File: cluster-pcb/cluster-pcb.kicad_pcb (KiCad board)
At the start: 4 copper layers, 60 x 160 mm, 77 parts, among them J1001 FFC_P1mm_BOT_RA_SMD, J1101 FFC_P1mm_BOT_RA_SMD, J501 FFC_P1mm_BOT_RA_SMD, J601 FFC_P1mm_BOT_RA_SMD, J701 FFC_P1mm_BOT_RA_SMD, J801 FFC_P1mm_BOT_RA_SMD, J901 FFC_P1mm_BOT_RA_SMD, Q301 MOSFET-N-CH-EN_100V_260mA, Q302 MOSFET-P-CH-EN_60V_50A, T301 TERM_BLK_HDR_2POS_90DEG_0.2IN, U1001 MAX13431E, U1101 MAX13431E, U301 TPSM365R6V5RDNR, U501 MAX13431E, U601 MAX13431E, U701 MAX13431E, U801 MAX13431E, U901 MAX13431E

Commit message: First steps towards v1.1
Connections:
- C303 pad 1: /VCC -> /power/VDD
- U301 pad 11: /VCC -> /power/VDD
- U301 pad 8: /VCC -> /power/VDD
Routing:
- net /VCC: track 160.5 -> 120.2 mm
- net /power/VDD: track 0.00 -> 12.8 mm
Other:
- board text added: "cluster-pcb v1.1 2024/08"
- board text removed: "cluster-pcb v1.0 2024/07"
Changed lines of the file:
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@@
   (title_block
     (title "cluster-pcb")
-    (date "2024-07-26")
-    (rev "1.0")
+    (date "2024-08-19")
+    (rev "1.1")
     (company "Howard Hughes Medical Institute")
   )
@@
   (net 77 "unconnected-(U301-BOOT-Pad7)")
   (net 78 "Net-(Q301-D)")
+  (net 79 "/power/VDD")
   (footprint "Janelia:FIDUCIAL_0.5mm_Mask1mm" (layer "F.Cu")
     (at 77.4 31.6)
@@
       (stroke (width 0.1) (type solid)) (layer "F.Fab"))
     (pad "1" smd roundrect (at -0.48 0 270) (size 0.56 0.62) (layers "F.Cu" "F.Paste" "F.Mask") (roundrect_rratio 0.25)
-      (net 43 "/VCC") (pintype "passive"))
+      (net 79 "/power/VDD") (pintype "passive"))
     (pad "2" smd roundrect (at 0.48 0 270) (size 0.56 0.62) (layers "F.Cu" "F.Paste" "F.Mask") (roundrect_rratio 0.25)
       (net 1 "/GND") (pintype "passive"))
@@
       (net 77 "unconnected-(U301-BOOT-Pad7)") (pinfunction "BOOT") (pintype "unspecified+no_connect"))
     (pad "8" smd rect (at 1.4 -1.962 270) (size 1.2 0.475) (layers "F.Cu")
-      (net 43 "/VCC") (pinfunction "VCC") (pintype "unspecified"))
+      (net 79 "/power/VDD") (pinfunction "VCC") (pintype "unspecified"))
     (pad "9" smd rect (at 0.499999 -2.049998 270) (size 0.349999 0.900001) (layers "F.Cu")
       (net 34 "/+5V") (pinfunction "BIAS") (pintype "unspecified"))
@@
       (net 1 "/GND") (pinfunction "GND") (pintype "power_in"))
     (pad "11" smd rect (at -0.499999 -2.049998 270) (size 0.349999 0.900001) (layers "F.Cu")
-      (net 43 "/VCC") (pinfunction "MODE_SYNC") (pintype "unspecified"))
+      (net 79 "/power/VDD") (pinfunction "MODE_SYNC") (pintype "unspecified"))
     (model "${KICAD_JANELIA_LIBRARY}/3dmodels/Janelia.3dshapes/TPSM365R6V5RDNR.step"
       (offset (xyz 0 0 0))
@@
     (effects (font (size 3 3) (thickness 0.75) bold))
   )
-  (gr_text "cluster-pcb\nv1.0 2024/07" (at 92.4 161.6) (layer "F.SilkS")
+  (gr_text "cluster-pcb\nv1.1 2024/08" (at 92.4 161.6) (layer "F.SilkS")
     (effects (font (size 2 2) (thickness 0.5) bold))
   )
@@
   (segment (start 107.12 36.56) (end 104.1925 33.6325) (width 0.6) (layer "F.Cu") (net 42))
   (segment (start 76.92 39.6) (end 76.92 40.12) (width 0.6) (layer "F.Cu") (net 42))
-  (segment (start 79.419999 43.100001) (end 80.4 42.12) (width 0.3) (layer "F.Cu") (net 43))
   (segment (start 110.4375 82.6) (end 110.4375 102.6) (width 2) (layer "F.Cu") (net 43))
   (segment (start 110.4375 102.6) (end 110.4375 122.6) (width 2) (layer "F.Cu") (net 43))
-  (segment (start 82.4 44.1) (end 82.4 43.1) (width 0.3) (layer "F.Cu") (net 43))
-  (segment (start 81.42 42.12) (end 80.4 42.12) (width 0.3) (layer "F.Cu") (net 43))
-  (segment (start 80.75 46.75) (end 82.4 45.1) (width 0.3) (layer "F.Cu") (net 43))
-  (segment (start 83.64 42.86) (end 109.4 42.86) (width 0.3) (layer "F.Cu") (net 43))
-  (segment (start 78.362 45) (end 78.362 45.981239) (width 0.3) (layer "F.Cu") (net 43))
   (segment (start 110.4375 48.6) (end 110.4375 62.6) (width 2) (layer "F.Cu") (net 43))
-  (segment (start 82.4 45.1) (end 82.4 44.1) (width 0.3) (layer "F.Cu") (net 43))
-  (segment (start 82.4 44.1) (end 83.64 42.86) (width 0.3) (layer "F.Cu") (net 43))
-  (segment (start 82.4 43.1) (end 81.42 42.12) (width 0.3) (layer "F.Cu") (net 43))
-  (segment (start 79.130761 46.75) (end 80.75 46.75) (width 0.3) (layer "F.Cu") (net 43))
   (segment (start 110.4375 48.6) (end 110.4375 43.8975) (width 2) (layer "F.Cu") (net 43))
   (segment (start 110.4375 43.8975) (end 109.4 42.86) (width 2) (layer "F.Cu") (net 43))
-  (segment (start 78.362 45.981239) (end 79.130761 46.75) (width 0.3) (layer "F.Cu") (net 43))
   (segment (start 110.4375 122.6) (end 110.4375 142.6) (width 2) (layer "F.Cu") (net 43))
   (segment (start 110.4375 142.6) (end 110.4375 162.6) (width 2) (layer "F.Cu") (net 43))
   (segment (start 110.4375 62.6) (end 110.4375 82.6) (width 2) (layer "F.Cu") (net 43))
-  (segment (start 78.449998 43.100001) (end 79.419999 43.100001) (width 0.3) (layer "F.Cu") (net 43))
   (segment (start 122.320001 30.5337) (end 120.479999 30.5337) (width 2) (layer "F.Cu") (net 44))
   (segment (start 120.479999 30.5337) (end 114.7188 30.5337) (width 2) (layer "F.Cu") (net 44))
@@
   (segment (start 78.4625 65.0475) (end 79.4 64.11) (width 0.3) (layer "F.Cu") (net 78))
   (segment (start 78.4625 66.6) (end 78.4625 65.0475) (width 0.3) (layer "F.Cu") (net 78))
+  (segment (start 79.419999 43.100001) (end 80.4 42.12) (width 0.3) (layer "F.Cu") (net 79))
+  (segment (start 82.4 44.1) (end 82.4 43.1) (width 0.3) (layer "F.Cu") (net 79))
+  (segment (start 81.42 42.12) (end 80.4 42.12) (width 0.3) (layer "F.Cu") (net 79))
+  (segment (start 80.75 46.75) (end 82.4 45.1) (width 0.3) (layer "F.Cu") (net 79))
+  (segment (start 78.362 45) (end 78.362 45.981239) (width 0.3) (layer "F.Cu") (net 79))
+  (segment (start 82.4 45.1) (end 82.4 44.1) (width 0.3) (layer "F.Cu") (net 79))
+  (segment (start 82.4 43.1) (end 81.42 42.12) (width 0.3) (layer "F.Cu") (net 79))
+  (segment (start 79.130761 46.75) (end 80.75 46.75) (width 0.3) (layer "F.Cu") (net 79))
+  (segment (start 78.362 45.981239) (end 79.130761 46.75) (width 0.3) (layer "F.Cu") (net 79))
+  (segment (start 78.449998 43.100001) (end 79.419999 43.100001) (width 0.3) (layer "F.Cu") (net 79))
   (zone (net 43) (net_name "/VCC") (layer "F.Cu") (hatch edge 0.5)
     (priority 2)

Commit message: Update to version 1.1
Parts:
- removed D1001, D1101, D501, D601, D701, D801, D901: D_Zener_47V_1W, Janelia:D_SMA
- removed D1002, D1102, D502, D602, D702, D802, D902: D, Janelia:D_SMB
- removed R1001, R1101, R501, R601, R701, R801, R901: 0.24, Janelia:R_2512_6332Metric
- added C305: 47uF_10V, Janelia:C_0805_2012Metric, F.Cu at (76.4, 49.1)
- added D302: LED_RED, Janelia:LED_0402-1005_KNB, F.Cu at (123.9, 23.4)
- added R303: 2.32k, Janelia:R_0805_2012Metric, F.Cu at (121.2, 23.4)
- Q301: value MOSFET-N-CH-EN_100V_260mA -> Transistor_BJT_NPN
- R301: value 1k -> 10.0k
- R302: value 3.6k -> 2.7k
- moved C304 4.72 mm to (76.4, 47.1), turned to 0 degrees
- moved C301 3.91 mm to (80.4, 39.1), turned to -90 degrees
- moved C303 3.04 mm to (79.9, 45.6), turned to 90 degrees
- moved Q301 2.00 mm to (79.4, 68.6), turned to -90 degrees
- moved R302 1.50 mm to (79.4, 65.1), turned to 0 degrees
- moved C1001 1.00 mm to (121.4, 114.6)
- moved C1002 1.00 mm to (123.4, 114.6)
- moved C1101 1.00 mm to (121.4, 154.6)
- moved C1102 1.00 mm to (123.4, 154.6)
- moved C501 1.00 mm to (121.4, 34.6)
- moved C502 1.00 mm to (123.4, 34.6)
- moved C601 1.00 mm to (121.4, 54.6)
- moved C602 1.00 mm to (123.4, 54.6)
- moved C701 1.00 mm to (121.4, 74.6)
- moved C702 1.00 mm to (123.4, 74.6)
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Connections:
- J1001 pad 1: /prism-4/VCC -> /VCC
- J1001 pad 2: /prism-4/VCC -> /VCC
- J1001 pad 3: /prism-4/VCC -> /VCC
- J1001 pad 4: /prism-4/VCC -> /VCC
- J1101 pad 1: /prism-6/VCC -> /VCC
- J1101 pad 2: /prism-6/VCC -> /VCC
- J1101 pad 3: /prism-6/VCC -> /VCC
- J1101 pad 4: /prism-6/VCC -> /VCC
- J501 pad 1: /prism-0/VCC -> /VCC
- J501 pad 2: /prism-0/VCC -> /VCC
- J501 pad 3: /prism-0/VCC -> /VCC
- J501 pad 4: /prism-0/VCC -> /VCC
- J601 pad 1: /prism-1/VCC -> /VCC
- J601 pad 2: /prism-1/VCC -> /VCC
- J601 pad 3: /prism-1/VCC -> /VCC
- J601 pad 4: /prism-1/VCC -> /VCC
- J701 pad 1: /prism-2/VCC -> /VCC
- J701 pad 2: /prism-2/VCC -> /VCC
- J701 pad 3: /prism-2/VCC -> /VCC
- J701 pad 4: /prism-2/VCC -> /VCC
- J801 pad 1: /prism-3/VCC -> /VCC
- J801 pad 2: /prism-3/VCC -> /VCC
- J801 pad 3: /prism-3/VCC -> /VCC
- J801 pad 4: /prism-3/VCC -> /VCC
- J901 pad 1: /prism-5/VCC -> /VCC
- J901 pad 2: /prism-5/VCC -> /VCC
- J901 pad 3: /prism-5/VCC -> /VCC
- J901 pad 4: /prism-5/VCC -> /VCC
- Q301 pad 2: /GND -> Net-(Q301-E)
- Q301 pad 3: Net-(Q301-D) -> /power/~{ENABLE_VCC}
- R302 pad 1: /power/~{ENABLE_VCC} -> Net-(Q301-E)
- R302 pad 2: Net-(Q301-D) -> /GND
- U1001 pad 7: (no net) -> /GND
- U1101 pad 7: (no net) -> /GND
- U501 pad 7: (no net) -> /GND
- U601 pad 7: (no net) -> /GND
- U701 pad 7: (no net) -> /GND
- U801 pad 7: (no net) -> /GND
- U901 pad 7: (no net) -> /GND
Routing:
- net /VCC: track 120.2 -> 263.2 mm
- net /+5V: track 263.8 -> 189.2 mm, vias 9 -> 8
- net /power/VBB: track 66.0 -> 38.2 mm
- net /GND: track 631.7 -> 656.5 mm, vias 31 -> 36
- net /prism-0/VCC: track 17.1 -> 0.00 mm
- net /prism-6/VCC: track 17.1 -> 0.00 mm
- net /prism-5/VCC: track 17.1 -> 0.00 mm
- net /prism-4/VCC: track 17.1 -> 0.00 mm
- net /prism-3/VCC: track 17.1 -> 0.00 mm
- net /prism-2/VCC: track 17.1 -> 0.00 mm
- net /prism-1/VCC: track 17.1 -> 0.00 mm
- net /prism-0/VBB: track 9.26 -> 0.00 mm
- net /+3.3V: track 186.5 -> 179.0 mm
- net /prism-4/VBB: track 7.10 -> 0.00 mm
- net /prism-3/VBB: track 7.10 -> 0.00 mm
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- added copper zone on In1.Cu, net /+3.3V
- added copper zone on F.Cu, net /+5V
- added copper zone on In2.Cu, net /+5V
- added copper zone on F.Cu, net /GND
- removed copper zone on In1.Cu, net /GND
- removed copper zone on In2.Cu, net /GND
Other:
- board text added: "+VDC"
- board text added: "ENABLE_VCC"
- board text added: "ETX0"
- board text added: "ETX1"
- board text added: "ETX2"
- board text added: "ETX3"
- board text added: "ETX4"
- board text added: "ETX5"
- board text added: "ETX6"
- board text added: "VCC"
- board text added: "VSYS"
- board text added: "~{ERX0}"
- board text added: "~{ERX1}"
- board text added: "~{ERX2}"
- board text added: "~{ERX3}"
- board text added: "~{ERX4}"
- board text added: "~{ERX5}"
- board text added: "~{ERX6}"
- board text removed: "+48VDC"

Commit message: Update documentation
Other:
- board text added: "+46VDC"
- board text removed: "+VDC"
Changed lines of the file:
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@@
         (effects (font (size 0.5 0.5) (thickness 0.125)))
     )
-    (fp_text value "3.3uF_50V" (at 0 2 90) (layer "F.Fab")
+    (fp_text value "3.3uF_50V" (at -3.75 0 90) (layer "F.Fab")
         (effects (font (size 0.5 0.5) (thickness 0.125)))
     )
@@
         (effects (font (size 0.5 0.5) (thickness 0.125) bold))
     )
-    (fp_text user "${REFERENCE}" (at -1.25 0) (layer "F.Fab")
+    (fp_text user "${REFERENCE}" (at 1.25 0) (layer "F.Fab")
         (effects (font (size 0.26 0.26) (thickness 0.065) bold))
     )
@@
         (effects (font (size 0.5 0.5) (thickness 0.125) bold))
     )
-    (fp_text value "Transistor_BJT_NPN" (at 1.25 0) (layer "F.Fab")
+    (fp_text value "Transistor_BJT_NPN" (at 0 2 90) (layer "F.Fab")
         (effects (font (size 0.5 0.5) (thickness 0.125) bold))
     )
@@
     (fp_line (start 1 0.625) (end -1 0.625)
       (stroke (width 0.1) (type solid)) (layer "F.Fab"))
-    (pad "1" smd roundrect (at -0.9125 0) (size 1.025 1.4) (layers "F.Cu" "F.Paste" "F.Mask") (roundrect_rratio 0.243902)
+    (pad "1" smd roundrect (at -0.9125 0) (size 1.025 1.4) (layers "F.Cu" "F.Paste" "F.Mask") (roundrect_rratio 0.243902439)
       (net 42 "/power/VBB") (pintype "passive"))
-    (pad "2" smd roundrect (at 0.9125 0) (size 1.025 1.4) (layers "F.Cu" "F.Paste" "F.Mask") (roundrect_rratio 0.243902)
+    (pad "2" smd roundrect (at 0.9125 0) (size 1.025 1.4) (layers "F.Cu" "F.Paste" "F.Mask") (roundrect_rratio 0.243902439)
       (net 45 "/power/LED_RED+") (pintype "passive"))
     (model "${KICAD_JANELIA_LIBRARY}/3dmodels/Janelia.3dshapes/R_0805_2012Metric.step"
@@
         (effects (font (size 0.5 0.5) (thickness 0.125) bold))
     )
-    (fp_text value "0.1uF_100V" (at 0 0.75 90) (layer "F.Fab")
+    (fp_text value "0.1uF_100V" (at -3 0 90) (layer "F.Fab")
         (effects (font (size 0.5 0.5) (thickness 0.125) bold))
     )
@@
         (effects (font (size 0.5 0.5) (thickness 0.125) bold))
     )
-    (fp_text value "1uF_25V" (at 3.25 0) (layer "F.Fab")
+    (fp_text value "1uF_25V" (at -2.25 0) (layer "F.Fab")
         (effects (font (size 0.5 0.5) (thickness 0.125) bold))
     )
@@
     (effects (font (size 0.75 0.75) (thickness 0.1875) bold))
   )
-  (gr_text "+VDC" (at 114.65 33.6) (layer "F.SilkS")
+  (gr_text "+46VDC" (at 114.65 33.6) (layer "F.SilkS")
     (effects (font (size 1 1) (thickness 0.25) bold))
   )

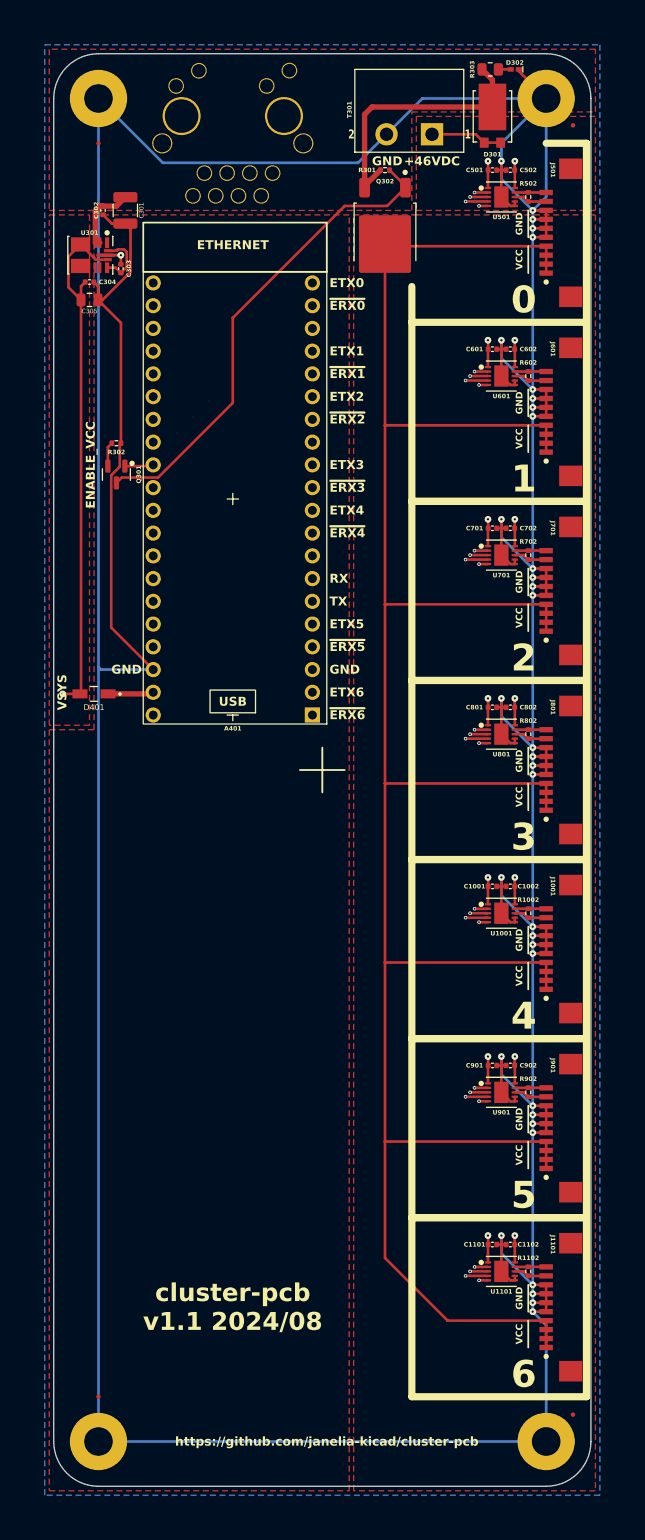
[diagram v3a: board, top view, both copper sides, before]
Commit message: Rearrange footprints
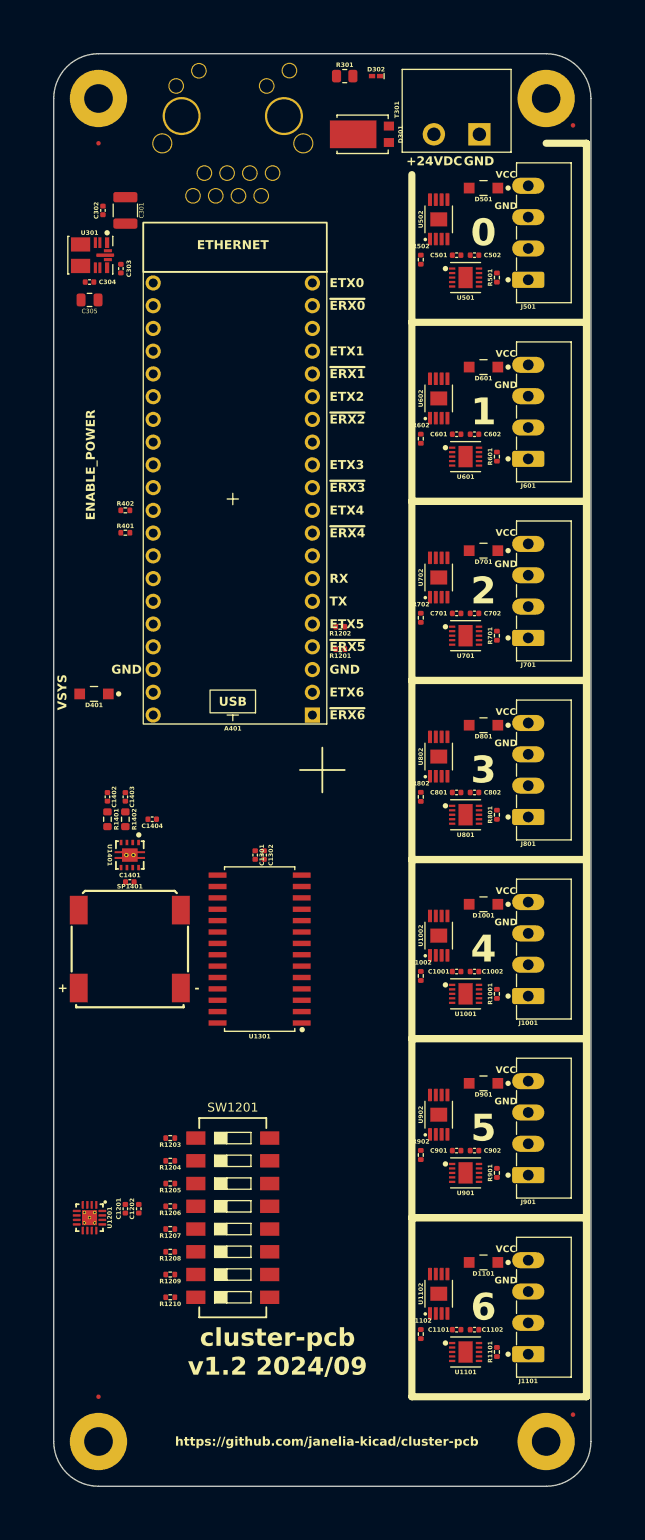
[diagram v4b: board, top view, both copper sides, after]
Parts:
- removed Q301: Transistor_BJT_NPN, Janelia:SOT-23
- removed Q302: MOSFET-P-CH-EN_60V_50A, Janelia:TO-252-2
- removed R302: 2.7k, Janelia:R_0402_1005Metric
- removed R303: 2.32k, Janelia:R_0805_2012Metric
- added C1201: 0.1uF_100V, Janelia:C_0402_1005Metric, F.Cu at (80.4, 150.6)
- added C1202: 0.1uF_100V, Janelia:C_0402_1005Metric, F.Cu at (81.9, 150.6)
- added C1301: 0.1uF_100V, Janelia:C_0402_1005Metric, F.Cu at (94.9, 111.1)
- added C1302: 1uF_35V, Janelia:C_0402_1005Metric, F.Cu at (95.9, 111.1)
- added C1401: 1uF_35V, Janelia:C_0402_1005Metric, F.Cu at (80.9, 114.1)
- added C1402: 0.22uF_25V, Janelia:C_0402_1005Metric, F.Cu at (78.4, 104.6)
- added C1403: 0.22uF_25V, Janelia:C_0402_1005Metric, F.Cu at (80.4, 104.6)
- added C1404: 0.22uF_25V, Janelia:C_0402_1005Metric, F.Cu at (83.4, 107.1)
- added D1001: D_SCHOTTKY_20V_1A, Janelia:SOD-123FL, F.Cu at (120.4, 116.6)
- added D1101: D_SCHOTTKY_20V_1A, Janelia:SOD-123FL, F.Cu at (120.4, 156.6)
- added D501: D_SCHOTTKY_20V_1A, Janelia:SOD-123FL, F.Cu at (120.4, 36.6)
- added D601: D_SCHOTTKY_20V_1A, Janelia:SOD-123FL, F.Cu at (120.4, 56.6)
- added D701: D_SCHOTTKY_20V_1A, Janelia:SOD-123FL, F.Cu at (120.4, 77.1)
- added D801: D_SCHOTTKY_20V_1A, Janelia:SOD-123FL, F.Cu at (120.4, 96.6)
- added D901: D_SCHOTTKY_20V_1A, Janelia:SOD-123FL, F.Cu at (120.4, 136.6)
- added R1001: 120, Janelia:R_0402_1005Metric, F.Cu at (121.9, 126.6)
- added R1101: 120, Janelia:R_0402_1005Metric, F.Cu at (121.9, 166.6)
- added R1201: 10.0k, Janelia:R_0402_1005Metric, F.Cu at (104.4, 88.1)
- added R1202: 10.0k, Janelia:R_0402_1005Metric, F.Cu at (104.4, 85.6)
- added R1203: 10.0k, Janelia:R_0402_1005Metric, F.Cu at (85.4, 142.7)
- added R1204: 10.0k, Janelia:R_0402_1005Metric, F.Cu at (85.4, 145.2)
- added R1205: 10.0k, Janelia:R_0402_1005Metric, F.Cu at (85.4, 147.8)
- added R1206: 10.0k, Janelia:R_0402_1005Metric, F.Cu at (85.4, 150.3)
- added R1207: 10.0k, Janelia:R_0402_1005Metric, F.Cu at (85.4, 152.9)
- added R1208: 10.0k, Janelia:R_0402_1005Metric, F.Cu at (85.4, 155.4)
- added R1209: 10.0k, Janelia:R_0402_1005Metric, F.Cu at (85.4, 157.9)
- added R1210: 10.0k, Janelia:R_0402_1005Metric, F.Cu at (85.4, 160.5)
- added R1401: 40k, Janelia:R_0603_1608Metric, F.Cu at (78.4, 107.1)
- added R1402: 40k, Janelia:R_0603_1608Metric, F.Cu at (80.4, 107.1)
- added R401: 1.8k, Janelia:R_0402_1005Metric, F.Cu at (80.4, 75.1)
- added R402: 1.8k, Janelia:R_0402_1005Metric, F.Cu at (80.4, 72.6)
- added R501: 120, Janelia:R_0402_1005Metric, F.Cu at (121.9, 46.6)
- added R601: 120, Janelia:R_0402_1005Metric, F.Cu at (121.9, 66.6)
- added R701: 120, Janelia:R_0402_1005Metric, F.Cu at (121.9, 86.6)
- added R801: 120, Janelia:R_0402_1005Metric, F.Cu at (121.9, 106.6)
- added R901: 120, Janelia:R_0402_1005Metric, F.Cu at (121.9, 146.6)
- added SP1401: Speaker_13x13mm_8Ohm_700mW, Janelia:Speaker_13x13mm_KLJ-01304T-08R07W, F.Cu at (80.9, 121.6)
- added SW1201: SW_DIP_x08_SDA08H1SBDR, Janelia:SW_DIP_SPSTx08_Slide_SDA08H1SBDR, F.Cu at (92.4, 151.6)
- added U1002: TPS1H200AQDGNRQ1, Janelia:SOP65P490X110-9N, F.Cu at (115.4, 120.1)
- added U1102: TPS1H200AQDGNRQ1, Janelia:SOP65P490X110-9N, F.Cu at (115.4, 160.1)
- added U1201: TCA6408ARGTR, Janelia:QFN50P300X300X100-17N, F.Cu at (76.4, 151.6)
- added U1301: MUX507, Janelia:DW28_TEX, F.Cu at (95.4, 121.6)
- added U1401: TPA6204A1DRBR, Janelia:DRB8_1P75X1P5, F.Cu at (80.9, 111.1)
- added U502: TPS1H200AQDGNRQ1, Janelia:SOP65P490X110-9N, F.Cu at (115.4, 40.1)
- added U602: TPS1H200AQDGNRQ1, Janelia:SOP65P490X110-9N, F.Cu at (115.4, 60.1)
- added U702: TPS1H200AQDGNRQ1, Janelia:SOP65P490X110-9N, F.Cu at (115.4, 80.1)
- added U802: TPS1H200AQDGNRQ1, Janelia:SOP65P490X110-9N, F.Cu at (115.4, 100.1)
- added U902: TPS1H200AQDGNRQ1, Janelia:SOP65P490X110-9N, F.Cu at (115.4, 140.1)
- D401: footprint Janelia:DIOM3616X98N -> Janelia:SOD-123FL
- J1001, J1101, J501, J601, J701, J801, J901: value FFC_P1mm_BOT_RA_SMD -> Conn_01x04_P3.5mm_TBH_Horizontal_Screw; footprint Janelia:CONN_C2914097 -> Janelia:PhoenixContact_MC_1,5_4-G-3.5_1x04_P3.50mm_Horizontal_Screw
- R1002, R1102, R502, R602, R702, R802, R902: value 100 -> 4.7k
- R301: value 10.0k -> 2.32k; footprint Janelia:R_0402_1005Metric -> Janelia:R_0805_2012Metric
- U1001, U1101, U501, U601, U701, U801, U901: value MAX13431E -> Interface_RS485_MAX13431E
- moved D302 15.5 mm to (108.4, 24.1)
- moved D301 14.6 mm to (106.9, 30.6), turned to 90 degrees
- moved R1002 13.9 mm to (113.4, 124.6)
- moved R1102 13.9 mm to (113.4, 164.6)
- moved R502 13.9 mm to (113.4, 44.6)
- moved R702 13.9 mm to (113.4, 84.6)
- moved R802 13.9 mm to (113.4, 104.6)
- moved R902 13.9 mm to (113.4, 144.6)
- moved R602 13.9 mm to (113.4, 64.6)
- moved R301 11.4 mm to (104.9, 24.1)
- moved C1101 10.3 mm to (117.4, 164.1)
- moved C1102 10.3 mm to (119.4, 164.1)
- moved C901 10.3 mm to (117.4, 144.1)
- moved C902 10.3 mm to (119.4, 144.1)
- moved C1001 10.3 mm to (117.4, 124.1)
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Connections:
- net /power/VBB renamed /VAA
- A401 pad 1: /~{ENABLE_RX_6} -> unconnected-(A401-UART0-TX/I2C0-SDA/SPI0-RX/GP0-Pad1)
- A401 pad 10: /ENABLE_TX_4 -> /MUX_ADDRESS_1
- A401 pad 11: /~{ENABLE_RX_3} -> /MUX_ADDRESS_0
- A401 pad 12: /ENABLE_TX_3 -> /ENABLE_TXRX_6
- A401 pad 14: /~{ENABLE_RX_2} -> /ENABLE_TXRX_5
- A401 pad 15: /ENABLE_TX_2 -> /ENABLE_TXRX_4
- A401 pad 16: /~{ENABLE_RX_1} -> /ENABLE_TXRX_3
- A401 pad 17: /ENABLE_TX_1 -> /ENABLE_TXRX_2
- A401 pad 19: /~{ENABLE_RX_0} -> /ENABLE_TXRX_1
- A401 pad 2: /ENABLE_TX_6 -> unconnected-(A401-UART0-RX/I2C0-SCL/SPI0-CS/GP1-Pad2)
- A401 pad 20: /ENABLE_TX_0 -> /ENABLE_TXRX_0
- A401 pad 29: /ENABLE_VCC -> /ENABLE_POWER
- A401 pad 31: unconnected-(A401-I2C1-SDA/ADC0/GP26-Pad31) -> /SDA
- A401 pad 32: unconnected-(A401-I2C1-SCL/ADC1/GP27-Pad32) -> /SCL
- A401 pad 34: unconnected-(A401-ADC2/GP28-Pad34) -> /AUDIO
- A401 pad 4: /~{ENABLE_RX_5} -> /~{ADDRESS_RESET}
- A401 pad 5: /ENABLE_TX_5 -> /~{ADDRESS_INT}
- A401 pad 9: /~{ENABLE_RX_4} -> /MUX_ADDRESS_2
- J1001 pad 1: /VCC -> /prism-4/SWN
- J1001 pad 2: /VCC -> /prism-4/SWP
- J1001 pad 3: /VCC -> /GND
- J1001 pad 4: /VCC -> /prism-4/VCC
- J1101 pad 1: /VCC -> /prism-6/SWN
- J1101 pad 2: /VCC -> /prism-6/SWP
- J1101 pad 3: /VCC -> /GND
- J1101 pad 4: /VCC -> /prism-6/VCC
- J501 pad 1: /VCC -> /prism-0/SWN
- J501 pad 2: /VCC -> /prism-0/SWP
- J501 pad 3: /VCC -> /GND
- J501 pad 4: /VCC -> /prism-0/VCC
- J601 pad 1: /VCC -> /prism-1/SWN
- J601 pad 2: /VCC -> /prism-1/SWP
- J601 pad 3: /VCC -> /GND
- J601 pad 4: /VCC -> /prism-1/VCC
- J701 pad 1: /VCC -> /prism-2/SWN
- J701 pad 2: /VCC -> /prism-2/SWP
- J701 pad 3: /VCC -> /GND
- J701 pad 4: /VCC -> /prism-2/VCC
- J801 pad 1: /VCC -> /prism-3/SWN
- J801 pad 2: /VCC -> /prism-3/SWP
- J801 pad 3: /VCC -> /GND
- J801 pad 4: /VCC -> /prism-3/VCC
- J901 pad 1: /VCC -> /prism-5/SWN
- J901 pad 2: /VCC -> /prism-5/SWP
- J901 pad 3: /VCC -> /GND
- J901 pad 4: /VCC -> /prism-5/VCC
- R1002 pad 1: /prism-4/SWP -> /ENABLE_POWER
- R1002 pad 2: /prism-4/SWN -> Net-(U1002-IN)
- R1102 pad 1: /prism-6/SWP -> /ENABLE_POWER
- R1102 pad 2: /prism-6/SWN -> Net-(U1102-IN)
- R301 pad 2: /power/~{ENABLE_VCC} -> /power/LED_RED+
- R502 pad 1: /prism-0/SWP -> /ENABLE_POWER
- R502 pad 2: /prism-0/SWN -> Net-(U502-IN)
- R602 pad 1: /prism-1/SWP -> /ENABLE_POWER
- R602 pad 2: /prism-1/SWN -> Net-(U602-IN)
- R702 pad 1: /prism-2/SWP -> /ENABLE_POWER
- R702 pad 2: /prism-2/SWN -> Net-(U702-IN)
- R802 pad 1: /prism-3/SWP -> /ENABLE_POWER
- R802 pad 2: /prism-3/SWN -> Net-(U802-IN)
- R902 pad 1: /prism-5/SWP -> /ENABLE_POWER
- R902 pad 2: /prism-5/SWN -> Net-(U902-IN)
- T301 pad 1: /power/VAA -> /GND
- T301 pad 2: /GND -> /power/VAA
- U1001 pad 2: /RX -> /RX_4
- U1001 pad 3: /ENABLE_TX_4 -> /ENABLE_TXRX_4
- U1001 pad 4: /~{ENABLE_RX_4} -> /ENABLE_TXRX_4
- U1001 pad 5: /TX -> /TX_4
- U1101 pad 2: /RX -> /RX_6
- U1101 pad 3: /ENABLE_TX_6 -> /ENABLE_TXRX_6
- U1101 pad 4: /~{ENABLE_RX_6} -> /ENABLE_TXRX_6
- U1101 pad 5: /TX -> /TX_6
- U501 pad 2: /RX -> /RX_0
- U501 pad 3: /ENABLE_TX_0 -> /ENABLE_TXRX_0
- U501 pad 4: /~{ENABLE_RX_0} -> /ENABLE_TXRX_0
- U501 pad 5: /TX -> /TX_0
- U601 pad 2: /RX -> /RX_1
- U601 pad 3: /ENABLE_TX_1 -> /ENABLE_TXRX_1
- U601 pad 4: /~{ENABLE_RX_1} -> /ENABLE_TXRX_1
- U601 pad 5: /TX -> /TX_1
- U701 pad 2: /RX -> /RX_2
- U701 pad 3: /ENABLE_TX_2 -> /ENABLE_TXRX_2
- U701 pad 4: /~{ENABLE_RX_2} -> /ENABLE_TXRX_2
- U701 pad 5: /TX -> /TX_2
- U801 pad 2: /RX -> /RX_3
- U801 pad 3: /ENABLE_TX_3 -> /ENABLE_TXRX_3
- U801 pad 4: /~{ENABLE_RX_3} -> /ENABLE_TXRX_3
- U801 pad 5: /TX -> /TX_3
- U901 pad 2: /RX -> /RX_5
- U901 pad 3: /ENABLE_TX_5 -> /ENABLE_TXRX_5
- U901 pad 4: /~{ENABLE_RX_5} -> /ENABLE_TXRX_5
- U901 pad 5: /TX -> /TX_5
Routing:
- net /GND: track 656.5 -> 0.00 mm, vias 36 -> 0
- net /VCC: track 263.2 -> 0.00 mm
- net /+5V: track 189.2 -> 0.00 mm, vias 8 -> 0
- net /+3.3V: track 179.0 -> 0.00 mm, vias 7 -> 0
- net /RX: track 149.9 -> 0.00 mm, vias 7 -> 0
- net /TX: track 147.3 -> 0.00 mm, vias 7 -> 0
- net /ENABLE_TX_6: track 74.0 -> 0.00 mm, vias 1 -> 0
- net /~{ENABLE_RX_6}: track 73.5 -> 0.00 mm, vias 1 -> 0
- net /ENABLE_TX_5: track 61.6 -> 0.00 mm, vias 1 -> 0
- net /~{ENABLE_RX_5}: track 60.9 -> 0.00 mm, vias 1 -> 0
- net /ENABLE_TX_4: track 54.3 -> 0.00 mm, vias 1 -> 0
- net /power/~{ENABLE_VCC}: track 54.2 -> 0.00 mm
- net /~{ENABLE_RX_4}: track 52.5 -> 0.00 mm, vias 1 -> 0
- net /ENABLE_TX_3: track 39.4 -> 0.00 mm, vias 1 -> 0
- net /VAA: track 38.2 -> 0.00 mm
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- removed copper zone on In1.Cu, net /+3.3V
- removed copper zone on F.Cu, net /+5V
- removed copper zone on In2.Cu, net /+5V
- removed copper zone on B.Cu, net /GND
- removed copper zone on F.Cu, net /GND
- removed copper zone on F.Cu, net /VAA
- removed copper zone on F.Cu, net /VCC
- removed copper zone on F.Cu, net /power/VAA
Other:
- board text added: "+24VDC"
- board text added: "ENABLE_POWER"
- board text added: "cluster-pcb v1.2 2024/09"
- board text removed: "+46VDC"
- board text removed: "ENABLE_VCC"
- board text removed: "cluster-pcb v1.1 2024/08"
